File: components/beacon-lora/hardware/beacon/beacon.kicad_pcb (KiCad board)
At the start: 2 copper layers, 60 x 98 mm, 4 parts, among them J1 Conn_Coaxial_Small, U1 GY-NEO6MV2, U2 ESP32-S3-DEVKITC-1-N8R8, U3 RFM95W-915S2

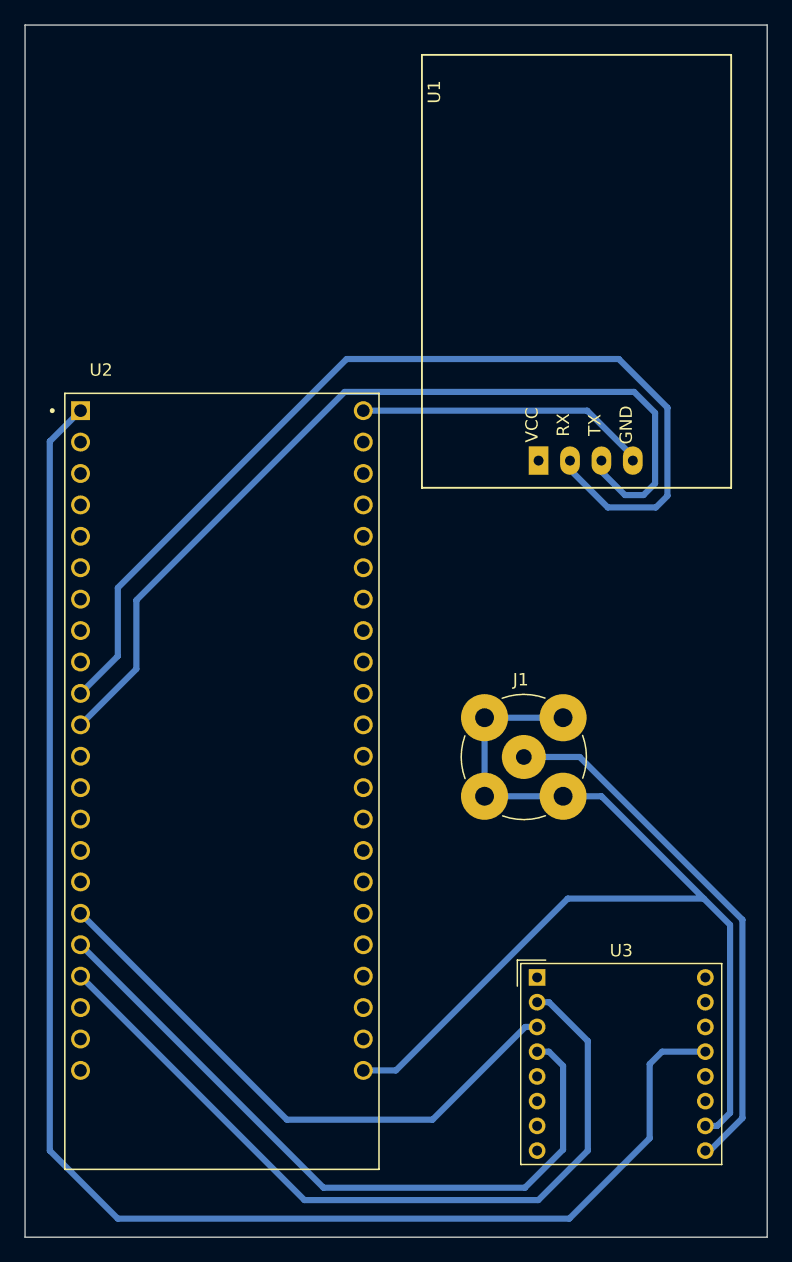
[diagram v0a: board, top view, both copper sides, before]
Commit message: Update on esp32 dimensions
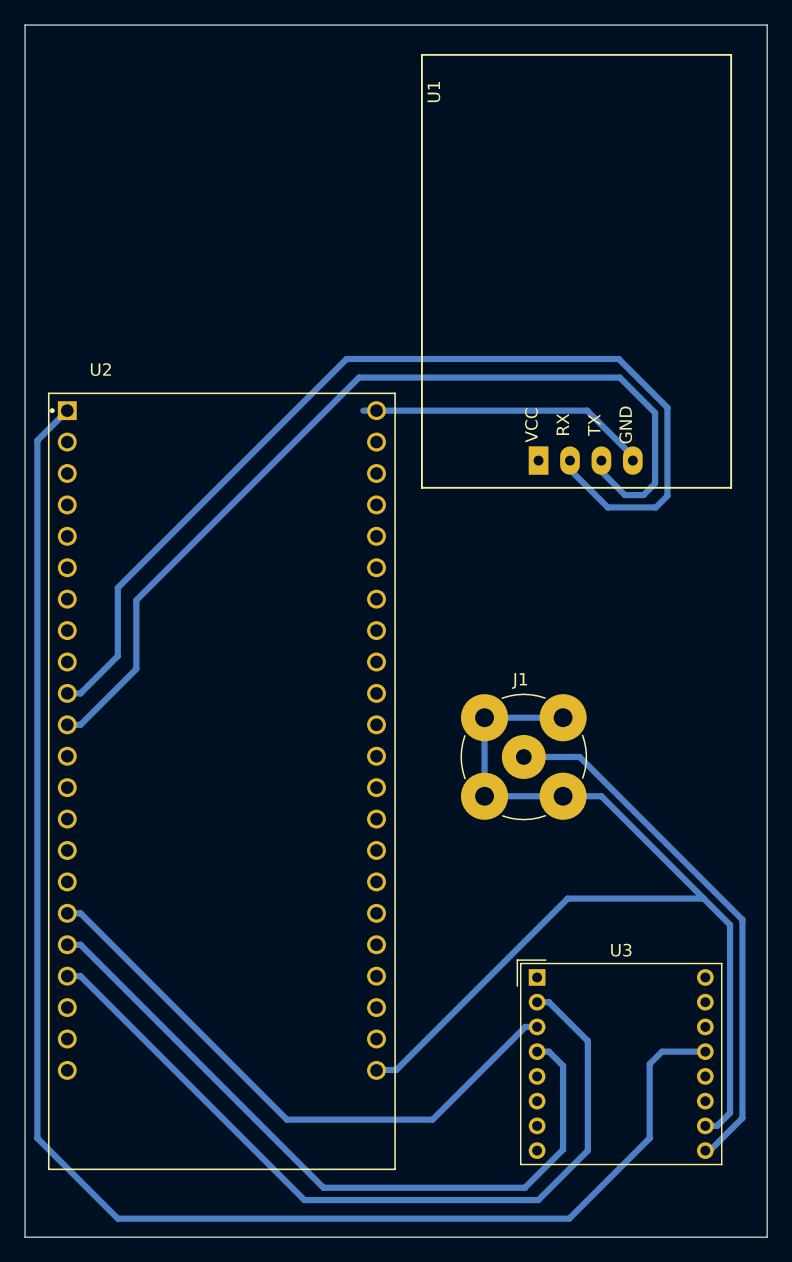
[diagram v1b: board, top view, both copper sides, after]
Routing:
- net Net-(U1-TX): track 73.7 -> 75.7 mm
- net Net-(J1-Ext): track 111.4 -> 110.3 mm
- net Net-(U1-RX): track 80.9 -> 82.0 mm
- net /SPI_SCK: track 57.8 -> 58.8 mm
- net /SPI_MOSI: track 46.9 -> 48.0 mm
- net /SPI_MISO: track 64.4 -> 65.5 mm
